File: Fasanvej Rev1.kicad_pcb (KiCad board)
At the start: 2 copper layers, 282 parts, among them J1 Molex 676430910, J10 I meas., J11 I meas., J12 USB4085-GF-A, J2 Molex 676430910, J3 LCD_RGB_40P, J4 Micro_SD_Card, J5 UART console, J6 Serial Wire Debug, J7 I meas., J8 I meas., J9 I meas., Q1 DMN2046U-7, Q2 DMN2046U-7, Q3 DMP2120U-7, SW1 TL3342F260QG, SW10 SW_Push, SW11 SW_Push, SW12 SW_Push, SW13 SW_Push, SW14 SW_Push, SW15 SW_Push, SW16 SW_Push, SW17 SW_Push, SW18 SW_Push, SW19 SW_Push, SW2 SW_Push, SW20 SW_Push, SW21 SW_Push, SW22 SW_Push, SW23 SW_Push, SW24 SW_Push, SW25 SW_Push, SW26 SW_Push, SW27 SW_Push, SW28 SW_Push, SW29 SW_Push, SW3 SW_Push, SW30 SW_Push, SW31 SW_Push, SW32 SW_Push, SW33 SW_Push, SW34 SW_Push, SW35 SW_Push, SW36 SW_Push, SW37 SW_Push, SW38 SW_Push, SW39 SW_Push, SW4 SW_Push, SW40 SW_Push, SW41 SW_Push, SW42 SW_Push, SW43 SW_Push, SW44 SW_Push, SW45 SW_Push, SW46 SW_Push, SW47 SW_Push, SW48 SW_Push, SW49 SW_Push, SW5 SW_Push, SW50 SW_Push, SW51 SW_Push, SW52 SW_Push, SW53 SW_Push, SW54 SW_Push, SW55 SW_Push, SW56 SW_Push, SW57 SW_Push, SW58 SW_Push, SW59 SW_Push, SW6 SW_Push, SW60 SW_Push, SW61 SW_Push, SW62 SW_Push, SW63 SW_Push, SW64 SW_Push, SW65 SW_Push, SW66 SW_SPST, SW67 SW_SPST, SW7 SW_Push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

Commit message: Started placing components
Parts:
- moved BT1 90.0 mm to (275.0, 85.0)
- moved BT2 90.0 mm to (297.5, 85.0)
- moved C1 90.0 mm to (137.5, 62.5)
- moved C10 90.0 mm to (138.4, 75.0)
- moved C11 90.0 mm to (145.0, 47.5)
- moved C12 90.0 mm to (137.5, 52.5)
- moved C13 90.0 mm to (147.5, 65.0)
- moved C14 90.0 mm to (139.0, 47.5)
- moved C15 90.0 mm to (142.5, 52.5)
- moved C16 90.0 mm to (137.5, 77.5)
- moved C17 90.0 mm to (149.1, 47.5)
- moved C18 90.0 mm to (150.0, 52.5)
- moved C19 90.0 mm to (137.5, 87.5)
- moved C2 90.0 mm to (145.0, 50.0)
- moved C20 90.0 mm to (147.5, 97.5)
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
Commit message: Made a lot of progress laying out PCB
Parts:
- removed the D16 at (49.7, 119.6)
- removed the D23 at (68.7, 98.5)
- removed the D24 at (116.7, 65.0)
- removed the D31 at (68.7, 101.4)
- removed the D32 at (102.9, 79.1)
- removed the D39 at (59.8, 117.3)
- removed the D40 at (59.1, 108.5)
- removed the D47 at (88.3, 89.1)
- removed the D48 at (74.3, 104.4)
- removed D55, D56, D63, D64: 1N4148, Diode_SMD:D_SOD-323_HandSoldering
- removed the D8 at (64.2, 108.5)
- removed the SW17 at (57.8, 58.2)
- removed the SW24 at (32.7, 80.3)
- removed the SW25 at (86.4, 58.2)
- removed the SW32 at (32.7, 108.5)
- removed the SW33 at (13.6, 113.0)
- removed the SW40 at (13.6, 84.8)
- removed the SW41 at (13.6, 98.9)
- removed the SW48 at (56.6, 72.3)
- removed the SW49 at (51.8, 114.6)
- removed SW56, SW57, SW64, SW65: SW_Push, Button_Switch_SMD:SW_SPST_TL3342
- removed the SW9 at (94.8, 65.3)
- removed TP2, TP3: TestPoint_Small, TestPoint:TestPoint_Pad_D4.0mm
- added J13: I2C keyboard, Connector_PinHeader_2.54mm:PinHeader_2x02_P2.54mm_Vertical, B.Cu at (72.5, 70.6)
- added R43: 4k7, Resistor_SMD:R_0603_1608Metric_Pad0.98x0.95mm_HandSolder, B.Cu at (76.1, 70.6)
- added R44: 4k7, Resistor_SMD:R_0603_1608Metric_Pad0.98x0.95mm_HandSolder, B.Cu at (76.1, 68.1)
- added R45: 22k, Resistor_SMD:R_0603_1608Metric_Pad0.98x0.95mm_HandSolder, F.Cu at (128.8, 15.7)
- BT1, BT2, C1, C10, C11, C12, C13, C14, C15, C16, C17, C18, C19, C2, C20, C22, C23, C24, C25, C26, C27, C28, C29, C3, C30, C31, C32, C33, C34, C35, C36, C37, C38, C39, C4, C40, C41, C42, C43, C44, C45, C46, C47, C5, C6, C7, C8, C9, FB1, J4, J5, J6, J7, J8, L1, L2, L3, L4, L5, LS1, Q1, Q2, Q3, R1, R2, R3, R4, R5, R6, R7, SW1, U1, U10, U11, U12, U13, U2, U3, U4, U5, U6, U7, U8, U9, Y1, Y2: moved to B.Cu
- C48: renamed from C49; moved to B.Cu
- C49: renamed from C50; moved to B.Cu
- C50: renamed from C51; moved to B.Cu
- C51: renamed from C52; moved to B.Cu
- C52: renamed from C53; moved to B.Cu
- C53: renamed from C54; moved to B.Cu
- D53: renamed from D66; moved to B.Cu
- D54: renamed from D67; moved to B.Cu
- J1: renamed from J2; moved to B.Cu
- J10: renamed from J9; moved to B.Cu
- J11: renamed from J10; moved to B.Cu
- J12: renamed from J11; moved to B.Cu
- J2: renamed from J1; moved to B.Cu
- J3: value LCD_RGB_40P -> LQ035NC111; footprint RISRES Library:TE_4-1734839-0_1x40-1MP_P0.5mm_Horizontal -> RISRES Library:FFC2B22-54-T
- J9: renamed from J12; moved to B.Cu
- R10: renamed from R8; moved to B.Cu
- R11: renamed from R9; moved to B.Cu
- R12: renamed from R10; moved to B.Cu
- R13: renamed from R11; moved to B.Cu
- R14: renamed from R12; moved to B.Cu
- R15: renamed from R13; moved to B.Cu
- R16: renamed from R40; moved to B.Cu
- R17: renamed from R41; moved to B.Cu
- R18: renamed from R14; moved to B.Cu
- R19: renamed from R42; moved to B.Cu
- R20: renamed from R15; moved to B.Cu
- R21: renamed from R16; moved to B.Cu
- R22: renamed from R38; moved to B.Cu
- R23: renamed from R39; moved to B.Cu
- R24: renamed from R17; moved to B.Cu
- R25: renamed from R18; moved to B.Cu
- R26: renamed from R19; moved to B.Cu
- R27: renamed from R20; moved to B.Cu
- R28: renamed from R21; moved to B.Cu
- R29: renamed from R22; moved to B.Cu
- R30: renamed from R23; moved to B.Cu
- R31: renamed from R24; moved to B.Cu
- R32: renamed from R25; moved to B.Cu
- R33: renamed from R26; moved to B.Cu
- R34: renamed from R27; moved to B.Cu
- R35: renamed from R28; moved to B.Cu
- R36: renamed from R29; moved to B.Cu
- R37: renamed from R30; moved to B.Cu
- R38: renamed from R31; moved to B.Cu
- R39: renamed from R32; moved to B.Cu
- R40: renamed from R33; moved to B.Cu
- R41: renamed from R34; moved to B.Cu
- R42: renamed from R35; moved to B.Cu
- R8: renamed from R36; moved to B.Cu
- R9: renamed from R37; moved to B.Cu
- SW10: renamed from SW11; value SW_Push -> W
- SW11: renamed from SW12; value SW_Push -> S
- SW12: renamed from SW13; value SW_Push -> X
- SW13: renamed from SW14; value SW_Push -> tab
- SW14: renamed from SW15; value SW_Push -> 0
- SW15: renamed from SW16; value SW_Push -> enter
- SW16: renamed from SW18; value SW_Push -> 3
- SW17: renamed from SW19; value SW_Push -> E
- SW18: renamed from SW20; value SW_Push -> D
- SW19: renamed from SW21; value SW_Push -> C
- SW2: value SW_Push -> 1
- SW20: renamed from SW22; value SW_Push -> caps lock
- SW21: renamed from SW23; value SW_Push -> O
- SW22: renamed from SW26; value SW_Push -> 4
- SW23: renamed from SW27; value SW_Push -> R
- SW24: renamed from SW28; value SW_Push -> F
- SW25: renamed from SW29; value SW_Push -> V
- SW26: renamed from SW30; value SW_Push -> ctrl
- SW27: renamed from SW31; value SW_Push -> P
- SW28: renamed from SW34; value SW_Push -> 5
- SW29: renamed from SW35; value SW_Push -> T
- SW3: value SW_Push -> Q
- SW30: renamed from SW36; value SW_Push -> G
- SW31: renamed from SW37; value SW_Push -> B
- SW32: renamed from SW38; value SW_Push -> space
- SW33: renamed from SW39; value SW_Push -> L
- SW34: renamed from SW42; value SW_Push -> 6
- SW35: renamed from SW43; value SW_Push -> Y
- SW36: renamed from SW44; value SW_Push -> H
- SW37: renamed from SW45; value SW_Push -> N
- SW38: renamed from SW46; value SW_Push -> space
- SW39: renamed from SW47; value SW_Push -> star
- SW4: value SW_Push -> A
- SW40: renamed from SW50; value SW_Push -> 7
- SW41: renamed from SW51; value SW_Push -> U
- SW42: renamed from SW52; value SW_Push -> J
- SW43: renamed from SW53; value SW_Push -> M
- SW44: renamed from SW54; value SW_Push -> empty
- SW45: renamed from SW55; value SW_Push -> point
- SW46: renamed from SW58; value SW_Push -> 8
- SW47: renamed from SW59; value SW_Push -> I
- SW48: renamed from SW60; value SW_Push -> K
- SW49: renamed from SW61; value SW_Push -> comma
- SW5: value SW_Push -> Z
- SW50: renamed from SW62; value SW_Push -> alt
- SW51: renamed from SW63; value SW_Push -> dash
- SW6: value SW_Push -> shift
- SW7: value SW_Push -> 9
- SW8: value SW_Push -> enter
- SW9: renamed from SW10; value SW_Push -> 2
- moved R16 252.6 mm to (13.8, 9.50), turned to 90 degrees
- moved J9 250.3 mm to (12.0, 6.53)
- moved R19 242.3 mm to (18.8, 8.50)
- moved R17 240.7 mm to (22.2, 3.75), turned to 180 degrees
- moved D52 237.7 mm to (26.6, 2.50)
- moved BT1 234.9 mm to (45.0, 37.5), turned to 180 degrees
- moved D51 228.9 mm to (30.6, 2.50)
- moved D6 218.8 mm to (200.5, 11.5), turned to -90 degrees
- moved H1 215.2 mm to (5.00, 5.00)
- moved R9 203.2 mm to (217.2, 51.8), turned to 180 degrees
- moved SW51 198.4 mm to (207.5, 50.0)
- moved R23 195.7 mm to (53.2, 2.50), turned to 180 degrees
- moved R22 194.3 mm to (49.8, 2.50)
- moved SW21 194.2 mm to (195.0, 25.0)
- moved Q3 194.0 mm to (50.8, 5.00), turned to 180 degrees
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- renumbered D11 to D10, D12 to D11, D13 to D12, D14 to D13, D15 to D14, D17 to D15, D18 to D16, D19 to D17, D20 to D18, D21 to D19, D22 to D20, D25 to D21, D26 to D22, D27 to D23, D28 to D24, D29 to D25, D30 to D26, D33 to D27, D34 to D28, D35 to D29, D36 to D30, D37 to D31, D38 to D32, D41 to D33, D42 to D34, D43 to D35, D44 to D36, D45 to D37, D46 to D38, D49 to D39, D50 to D40, D51 to D41, D52 to D42, D53 to D43, D54 to D44, D57 to D45, D58 to D46, D59 to D47, D60 to D48, D61 to D49, D62 to D50, D65 to D51, D68 to D52, D9 to D8, D10 to D9, SW67 to SW52, SW66 to SW53
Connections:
- C23 pad 1: Net-(C23-Pad1) -> /Keyboard/+3V3_SAMD21
- C24 pad 1: Net-(C23-Pad1) -> /Keyboard/+3V3_SAMD21
- C25 pad 1: Net-(C23-Pad1) -> /Keyboard/+3V3_SAMD21
- C26 pad 1: Net-(C23-Pad1) -> /Keyboard/+3V3_SAMD21
- C27 pad 1: Net-(C23-Pad1) -> /Keyboard/+3V3_SAMD21
- C28 pad 1: Net-(C23-Pad1) -> /Keyboard/+3V3_SAMD21
- C29 pad 1: Net-(C23-Pad1) -> /Keyboard/+3V3_SAMD21
- D1 pad 1: /Keyboard/ROW_1 -> /Keyboard/COLUMN_1
- D10 pad 1: /Keyboard/ROW_3 -> /Keyboard/COLUMN_3
- D11 pad 1: /Keyboard/ROW_4 -> /Keyboard/COLUMN_4
- D12 pad 1: /Keyboard/ROW_5 -> /Keyboard/COLUMN_5
- D13 pad 1: /Keyboard/ROW_6 -> /Keyboard/COLUMN_6
- D14 pad 1: /Keyboard/ROW_7 -> /Keyboard/COLUMN_7
- D15 pad 1: /Keyboard/ROW_1 -> /Keyboard/COLUMN_1
- D16 pad 1: /Keyboard/ROW_2 -> /Keyboard/COLUMN_2
- D17 pad 1: /Keyboard/ROW_3 -> /Keyboard/COLUMN_3
- D18 pad 1: /Keyboard/ROW_4 -> /Keyboard/COLUMN_4
- D19 pad 1: /Keyboard/ROW_5 -> /Keyboard/COLUMN_5
- D2 pad 1: /Keyboard/ROW_2 -> /Keyboard/COLUMN_2
- D20 pad 1: /Keyboard/ROW_6 -> /Keyboard/COLUMN_6
- D21 pad 1: /Keyboard/ROW_1 -> /Keyboard/COLUMN_1
- D22 pad 1: /Keyboard/ROW_2 -> /Keyboard/COLUMN_2
- D23 pad 1: /Keyboard/ROW_3 -> /Keyboard/COLUMN_3
- D24 pad 1: /Keyboard/ROW_4 -> /Keyboard/COLUMN_4
- D25 pad 1: /Keyboard/ROW_5 -> /Keyboard/COLUMN_5
- D26 pad 1: /Keyboard/ROW_6 -> /Keyboard/COLUMN_6
- D27 pad 1: /Keyboard/ROW_1 -> /Keyboard/COLUMN_1
- D28 pad 1: /Keyboard/ROW_2 -> /Keyboard/COLUMN_2
- D29 pad 1: /Keyboard/ROW_3 -> /Keyboard/COLUMN_3
- D3 pad 1: /Keyboard/ROW_3 -> /Keyboard/COLUMN_3
- D30 pad 1: /Keyboard/ROW_4 -> /Keyboard/COLUMN_4
- D31 pad 1: /Keyboard/ROW_5 -> /Keyboard/COLUMN_5
- D32 pad 1: /Keyboard/ROW_6 -> /Keyboard/COLUMN_6
- D33 pad 1: /Keyboard/ROW_1 -> /Keyboard/COLUMN_1
- D34 pad 1: /Keyboard/ROW_2 -> /Keyboard/COLUMN_2
- D35 pad 1: /Keyboard/ROW_3 -> /Keyboard/COLUMN_3
- D36 pad 1: /Keyboard/ROW_4 -> /Keyboard/COLUMN_4
- D37 pad 1: /Keyboard/ROW_5 -> /Keyboard/COLUMN_5
- D38 pad 1: /Keyboard/ROW_6 -> /Keyboard/COLUMN_6
- D39 pad 1: /Keyboard/ROW_1 -> /Keyboard/COLUMN_1
- D4 pad 1: /Keyboard/ROW_4 -> /Keyboard/COLUMN_4
- D40 pad 1: /Keyboard/ROW_2 -> /Keyboard/COLUMN_2
- D41 pad 1: /Keyboard/ROW_3 -> /Keyboard/COLUMN_3
- D42 pad 1: /Keyboard/ROW_4 -> /Keyboard/COLUMN_4
- D43 pad 1: /Keyboard/ROW_5 -> /Keyboard/COLUMN_5
- D44 pad 1: /Keyboard/ROW_6 -> /Keyboard/COLUMN_6
- D45 pad 1: /Keyboard/ROW_1 -> /Keyboard/COLUMN_1
- D46 pad 1: /Keyboard/ROW_2 -> /Keyboard/COLUMN_2
- D47 pad 1: /Keyboard/ROW_3 -> /Keyboard/COLUMN_3
- D48 pad 1: /Keyboard/ROW_4 -> /Keyboard/COLUMN_4
- D49 pad 1: /Keyboard/ROW_5 -> /Keyboard/COLUMN_5
- D5 pad 1: /Keyboard/ROW_5 -> /Keyboard/COLUMN_5
- D50 pad 1: /Keyboard/ROW_6 -> /Keyboard/COLUMN_6
- D6 pad 1: /Keyboard/ROW_6 -> /Keyboard/COLUMN_6
- D7 pad 1: /Keyboard/ROW_7 -> /Keyboard/COLUMN_7
- D8 pad 1: /Keyboard/ROW_1 -> /Keyboard/COLUMN_1
- D9 pad 1: /Keyboard/ROW_2 -> /Keyboard/COLUMN_2
- FB1 pad 2: Net-(C23-Pad1) -> /Keyboard/+3V3_SAMD21
- J1 pad 2: Net-(J2-Pad2) -> Net-(J1-Pad2)
- J1 pad 3: Net-(J2-Pad3) -> Net-(J1-Pad3)
- J3 pad 10: /LCD_D21 -> Net-(J3-Pad10)
- J3 pad 11: /LCD_D22 -> Net-(J3-Pad10)
- J3 pad 12: /LCD_D23 -> GND
- J3 pad 14: GND -> /LCD_D2
- J3 pad 15: /LCD_D10 -> /LCD_D3
- J3 pad 16: /LCD_D11 -> /LCD_D4
- J3 pad 17: /LCD_D12 -> /LCD_D5
- J3 pad 18: /LCD_D13 -> /LCD_D6
- J3 pad 19: /LCD_D14 -> /LCD_D7
- J3 pad 2: LED_BACKLIGHT_A -> LED_BACKLIGHT_K
- J3 pad 20: /LCD_D15 -> GND
- J3 pad 22: GND -> /LCD_D10
- J3 pad 23: /LCD_D2 -> /LCD_D11
- J3 pad 24: /LCD_D3 -> /LCD_D12
- J3 pad 25: /LCD_D4 -> /LCD_D13
- J3 pad 26: /LCD_D5 -> /LCD_D14
- J3 pad 27: /LCD_D6 -> /LCD_D15
- J3 pad 28: /LCD_D7 -> GND
- J3 pad 3: GND -> LED_BACKLIGHT_A
- J3 pad 30: /LCD_CLK -> /LCD_D23
- J3 pad 31: +3V3 -> /LCD_D22
- J3 pad 32: /LCD_HSYNC -> /LCD_D21
- J3 pad 33: /LCD_VSYNC -> /LCD_D20
- J3 pad 34: /LCD_DE -> /LCD_D19
- J3 pad 35: (no net) -> /LCD_D18
- J3 pad 36: GND -> /LCD_HSYNC
- J3 pad 37: /TPX1 -> /LCD_VSYNC
- J3 pad 38: /TPY1 -> /LCD_CLK
- J3 pad 39: /TPX2 -> unconnected-(J3-Pad39)
- J3 pad 4: +3V3 -> LED_BACKLIGHT_A
- J3 pad 40: /TPY2 -> unconnected-(J3-Pad40)
- J3 pad 5: GND -> unconnected-(J3-Pad5)
- J3 pad 6: GND -> unconnected-(J3-Pad6)
- J3 pad 7: /LCD_D18 -> unconnected-(J3-Pad7)
- J3 pad 8: /LCD_D19 -> Net-(J3-Pad10)
- J3 pad 9: /LCD_D20 -> Net-(J3-Pad10)
- J6 pad 1: +3V3 -> /Keyboard/+3V3_SAMD21
- R6 pad 1: +3V3 -> /Keyboard/+3V3_SAMD21
- R7 pad 1: +3V3 -> /Keyboard/+3V3_SAMD21
- R9 pad 1: +3V3 -> Net-(R9-Pad1)
- R9 pad 2: Net-(R37-Pad2) -> /Keyboard/+3V3_SAMD21
- SW10 pad 2: /Keyboard/COLUMN_2 -> /Keyboard/ROW_2
- SW11 pad 2: /Keyboard/COLUMN_2 -> /Keyboard/ROW_2
- SW12 pad 2: /Keyboard/COLUMN_2 -> /Keyboard/ROW_2
- SW13 pad 2: /Keyboard/COLUMN_2 -> /Keyboard/ROW_2
- SW14 pad 2: /Keyboard/COLUMN_2 -> /Keyboard/ROW_2
- SW15 pad 2: /Keyboard/COLUMN_2 -> /Keyboard/ROW_2
- SW16 pad 2: /Keyboard/COLUMN_3 -> /Keyboard/ROW_3
- SW17 pad 2: /Keyboard/COLUMN_3 -> /Keyboard/ROW_3
- SW18 pad 2: /Keyboard/COLUMN_3 -> /Keyboard/ROW_3
- SW19 pad 2: /Keyboard/COLUMN_3 -> /Keyboard/ROW_3
- SW2 pad 2: /Keyboard/COLUMN_1 -> /Keyboard/ROW_1
- SW20 pad 2: /Keyboard/COLUMN_3 -> /Keyboard/ROW_3
- SW21 pad 2: /Keyboard/COLUMN_3 -> /Keyboard/ROW_3
- SW22 pad 2: /Keyboard/COLUMN_4 -> /Keyboard/ROW_4
- SW23 pad 2: /Keyboard/COLUMN_4 -> /Keyboard/ROW_4
- SW24 pad 2: /Keyboard/COLUMN_4 -> /Keyboard/ROW_4
- SW25 pad 2: /Keyboard/COLUMN_4 -> /Keyboard/ROW_4
- SW26 pad 2: /Keyboard/COLUMN_4 -> /Keyboard/ROW_4
- SW27 pad 2: /Keyboard/COLUMN_4 -> /Keyboard/ROW_4
- SW28 pad 2: /Keyboard/COLUMN_5 -> /Keyboard/ROW_5
- SW29 pad 2: /Keyboard/COLUMN_5 -> /Keyboard/ROW_5
- SW3 pad 2: /Keyboard/COLUMN_1 -> /Keyboard/ROW_1
- SW30 pad 2: /Keyboard/COLUMN_5 -> /Keyboard/ROW_5
- SW31 pad 2: /Keyboard/COLUMN_5 -> /Keyboard/ROW_5
- SW32 pad 2: /Keyboard/COLUMN_5 -> /Keyboard/ROW_5
- SW33 pad 2: /Keyboard/COLUMN_5 -> /Keyboard/ROW_5
- SW34 pad 2: /Keyboard/COLUMN_6 -> /Keyboard/ROW_6
- SW35 pad 2: /Keyboard/COLUMN_6 -> /Keyboard/ROW_6
- SW36 pad 2: /Keyboard/COLUMN_6 -> /Keyboard/ROW_6
- SW37 pad 2: /Keyboard/COLUMN_6 -> /Keyboard/ROW_6
- SW38 pad 2: /Keyboard/COLUMN_6 -> /Keyboard/ROW_6
- SW39 pad 2: /Keyboard/COLUMN_6 -> /Keyboard/ROW_6
- SW4 pad 2: /Keyboard/COLUMN_1 -> /Keyboard/ROW_1
- SW40 pad 2: /Keyboard/COLUMN_7 -> /Keyboard/ROW_7
- SW41 pad 2: /Keyboard/COLUMN_7 -> /Keyboard/ROW_7
- SW42 pad 2: /Keyboard/COLUMN_7 -> /Keyboard/ROW_7
- SW43 pad 2: /Keyboard/COLUMN_7 -> /Keyboard/ROW_7
- SW44 pad 2: /Keyboard/COLUMN_7 -> /Keyboard/ROW_7
- SW45 pad 2: /Keyboard/COLUMN_7 -> /Keyboard/ROW_7
- SW46 pad 2: /Keyboard/COLUMN_8 -> /Keyboard/ROW_8
- SW47 pad 2: /Keyboard/COLUMN_8 -> /Keyboard/ROW_8
- SW48 pad 2: /Keyboard/COLUMN_8 -> /Keyboard/ROW_8
- SW49 pad 2: /Keyboard/COLUMN_8 -> /Keyboard/ROW_8
- SW5 pad 2: /Keyboard/COLUMN_1 -> /Keyboard/ROW_1
- SW50 pad 2: /Keyboard/COLUMN_8 -> /Keyboard/ROW_8
- SW51 pad 2: /Keyboard/COLUMN_8 -> /Keyboard/ROW_8
- SW52 pad 2: Net-(R37-Pad2) -> Net-(R9-Pad1)
- SW6 pad 2: /Keyboard/COLUMN_1 -> /Keyboard/ROW_1
- SW7 pad 2: /Keyboard/COLUMN_1 -> /Keyboard/ROW_1
- SW8 pad 2: /Keyboard/COLUMN_1 -> /Keyboard/ROW_1
- SW9 pad 2: /Keyboard/COLUMN_2 -> /Keyboard/ROW_2
- TP1 pad 1: /I2C_SCL -> /LCD_D11
- U2 pad 1: /USB_DM_EXTERNAL -> /USB_DP_EXTERNAL
- U2 pad 3: /USB_DP_EXTERNAL -> /USB_DM_EXTERNAL
- U2 pad 4: Net-(J2-Pad3) -> Net-(J1-Pad2)
- U2 pad 6: Net-(J2-Pad2) -> Net-(J1-Pad3)
- U4 pad 21: Net-(C23-Pad1) -> /Keyboard/+3V3_SAMD21
- U4 pad 34: Net-(C23-Pad1) -> /Keyboard/+3V3_SAMD21
- U4 pad 35: unconnected-(U4-Pad35) -> /KEYBOARD_S1_P0
- U4 pad 36: unconnected-(U4-Pad36) -> /KEYBOARD_S1_P1
- U4 pad 48: Net-(C23-Pad1) -> /Keyboard/+3V3_SAMD21
- U4 pad 55: Net-(C23-Pad1) -> /Keyboard/+3V3_SAMD21
- U4 pad 56: Net-(C23-Pad1) -> /Keyboard/+3V3_SAMD21
- U4 pad 8: Net-(C23-Pad1) -> /Keyboard/+3V3_SAMD21
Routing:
- net Net-(BT1-Pad2): track 0.00 -> 175.3 mm
- net /Keyboard/ROW_2: track 0.00 -> 147.8 mm, vias 0 -> 1
- net /Keyboard/ROW_1: track 0.00 -> 137.9 mm, vias 0 -> 1
- net /Keyboard/ROW_3: track 0.00 -> 115.4 mm, vias 0 -> 8
- net /Keyboard/ROW_4: track 0.00 -> 99.2 mm, vias 0 -> 8
- net /Keyboard/ROW_5: track 0.00 -> 97.2 mm, vias 0 -> 8
- net /Keyboard/+3V3_SAMD21: track 0.00 -> 70.7 mm
- net /USB_VBUS_EXTERNAL: track 0.00 -> 67.2 mm, vias 0 -> 1
- net GND: track 0.00 -> 51.1 mm, vias 0 -> 12
- net /Keyboard/COLUMN_5: track 0.00 -> 50.0 mm
- net /Keyboard/COLUMN_4: track 0.00 -> 50.0 mm
- net /Keyboard/COLUMN_3: track 0.00 -> 50.0 mm
- net /Keyboard/COLUMN_2: track 0.00 -> 50.0 mm
- net /Keyboard/COLUMN_1: track 0.00 -> 50.0 mm
- net /Keyboard/SWD_CLK: track 0.00 -> 45.6 mm, vias 0 -> 1
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- added copper zone on B.Cu, net +BATT
- added copper zone on B.Cu, net Net-(D54-Pad2)
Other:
- board outline added: 220 x 72.5 mm

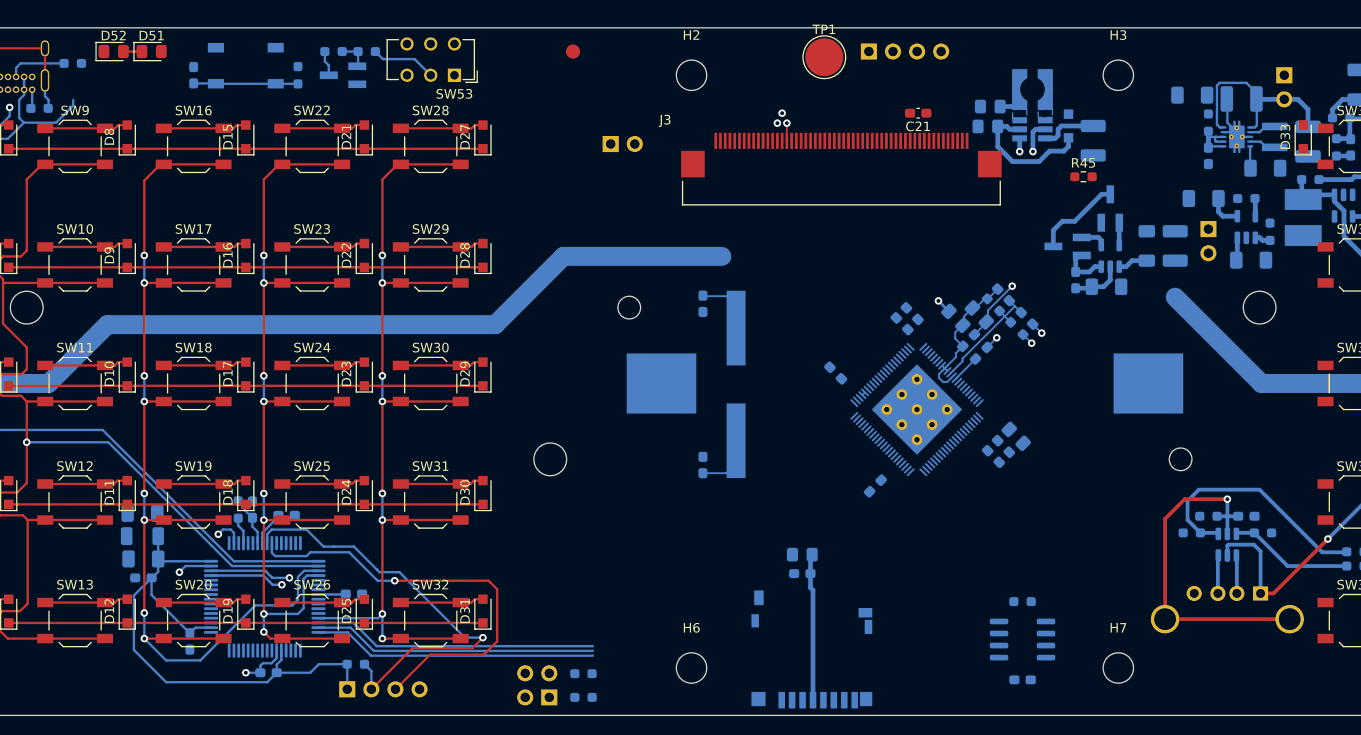
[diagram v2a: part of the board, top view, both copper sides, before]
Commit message: Made progress with board layout as well as mechanical (case) design
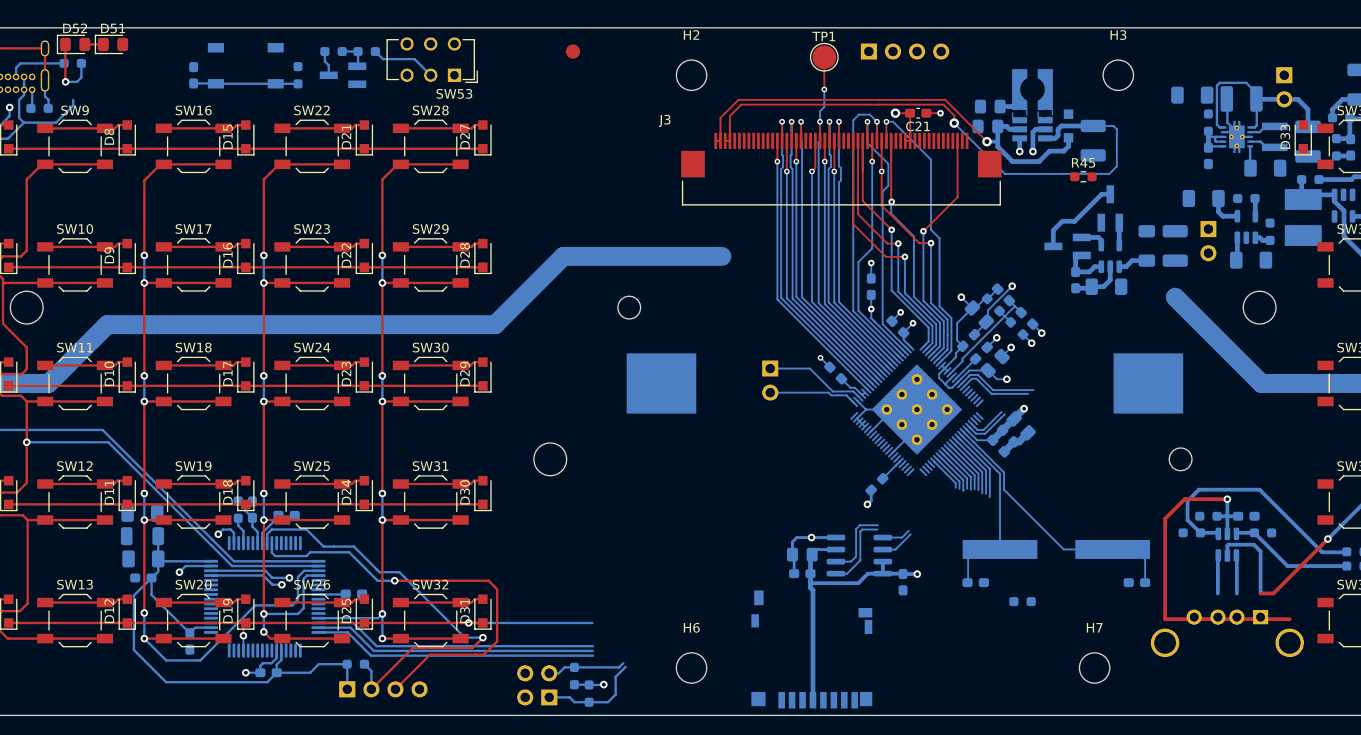
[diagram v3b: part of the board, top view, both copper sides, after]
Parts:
- TP1: footprint TestPoint:TestPoint_Pad_D4.0mm -> TestPoint:TestPoint_Pad_D2.5mm
- moved C6 47.4 mm to (134.5, 58.5), turned to 180 degrees
- moved C5 41.1 mm to (117.5, 58.5), turned to 0 degrees
- moved Y1 38.0 mm to (126.0, 55.0), turned to 180 degrees
- moved LS1 29.0 mm to (95.8, 35.9), turned to 180 degrees
- moved U3 19.3 mm to (105.2, 55.6), turned to 0 degrees
- moved C13 16.3 mm to (109.8, 58.5), turned to -90 degrees
- moved C12 6.31 mm to (119.5, 35.4), turned to -135 degrees
- moved C17 5.08 mm to (106.5, 27.3), turned to -90 degrees
- moved D51 4.14 mm to (26.5, 1.75)
- moved D52 4.14 mm to (22.5, 1.75)
- moved H7 2.50 mm to (130.0, 67.5)
- moved J1 2.50 mm to (147.5, 62.1)
- moved C7 2.07 mm to (109.2, 31.6)
- moved C14 1.22 mm to (122.3, 42.0)
- moved C16 1.22 mm to (119.8, 44.1)
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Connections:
- net Net-(C3-Pad2) renamed /RESET
- net Net-(C5-Pad1) renamed /HOSCO
- net Net-(C6-Pad1) renamed /HOSCI
- U1 pad 63: /TPY2 -> unconnected-(U1-Pad63)
- U1 pad 64: /TPY1 -> unconnected-(U1-Pad64)
- U1 pad 65: /TPX2 -> unconnected-(U1-Pad65)
- U1 pad 66: /TPX1 -> unconnected-(U1-Pad66)
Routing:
- net LED_BACKLIGHT_A: track 5.97 -> 60.8 mm, vias 0 -> 1
- net +3V3: track 15.9 -> 58.1 mm, vias 0 -> 5
- net GND: track 51.1 -> 91.7 mm, vias 12 -> 19
- net /LCD_D11: track 0.00 -> 38.3 mm, vias 0 -> 2
- net LED_BACKLIGHT_K: track 14.2 -> 49.1 mm, vias 0 -> 1
- net /LCD_D3: track 0.00 -> 34.0 mm
- net /LCD_D5: track 0.07 -> 33.3 mm, vias 0 -> 1
- net /LCD_D7: track 0.00 -> 32.4 mm, vias 0 -> 1
- net /LCD_D18: track 0.00 -> 32.1 mm, vias 0 -> 1
- net /LCD_VSYNC: track 0.00 -> 31.2 mm, vias 0 -> 1
- net /LCD_D13: track 0.00 -> 30.7 mm, vias 0 -> 1
- net /LCD_D2: track 0.00 -> 30.2 mm
- net /LCD_D15: track 0.00 -> 29.9 mm, vias 0 -> 1
- net /LCD_D6: track 0.00 -> 28.7 mm, vias 0 -> 1
- net /LCD_D20: track 0.00 -> 28.3 mm, vias 0 -> 1
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
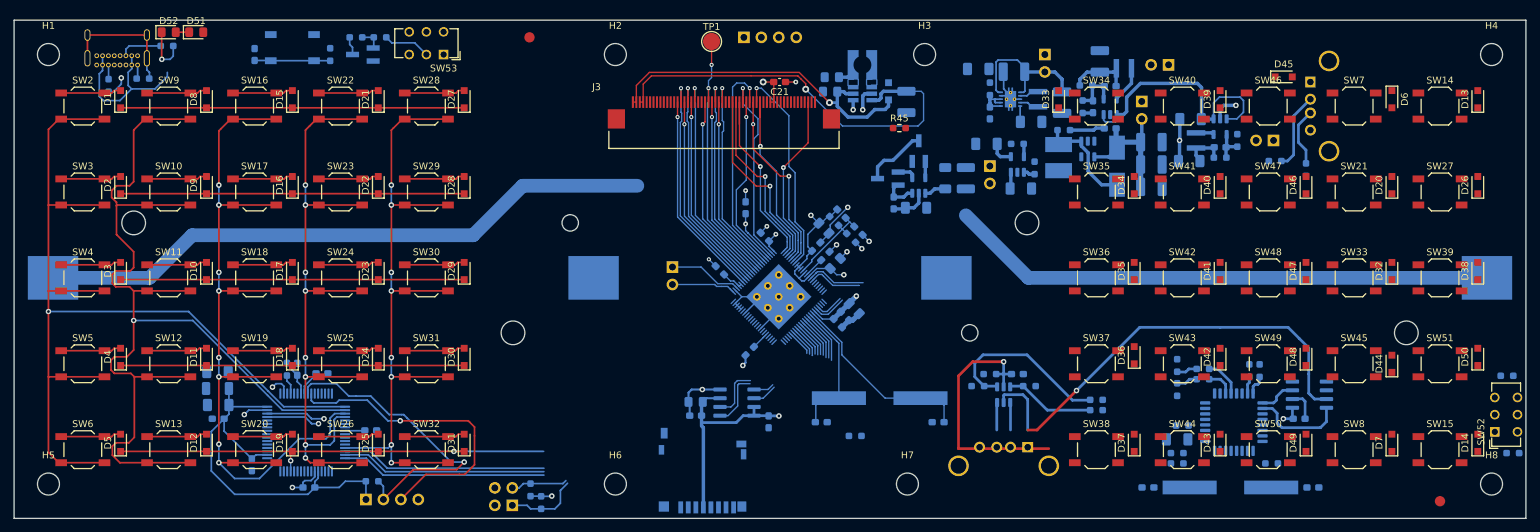
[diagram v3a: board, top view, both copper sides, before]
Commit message: Made progress with PCB layout. Preliminary case design added.
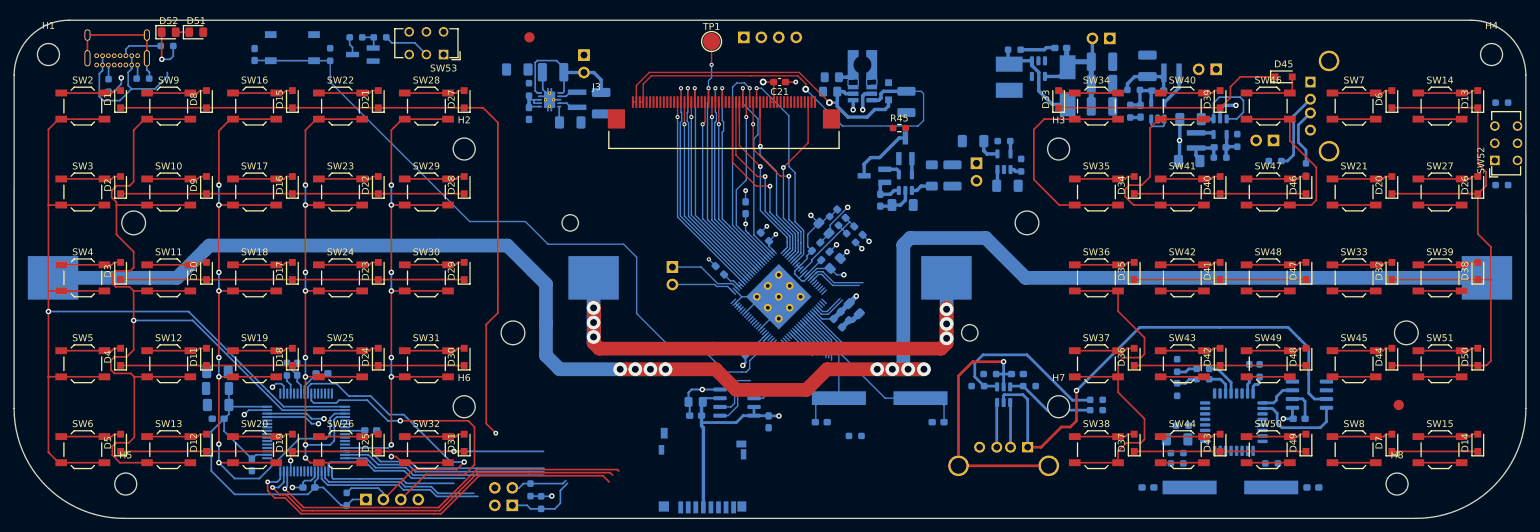
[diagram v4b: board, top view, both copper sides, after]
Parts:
- moved C37 67.1 mm to (73.2, 7.18)
- moved C31 67.1 mm to (80.9, 14.9)
- moved C32 67.1 mm to (74.9, 13.6)
- moved C34 67.1 mm to (78.4, 7.58)
- moved C36 67.1 mm to (85.4, 12.1)
- moved J8 67.1 mm to (82.9, 5.08)
- moved L1 67.1 mm to (81.9, 12.7)
- moved R10 67.1 mm to (74.9, 10.1)
- moved U6 67.1 mm to (77.9, 11.6)
- moved R9 39.8 mm to (216.5, 12.0)
- moved SW52 39.5 mm to (215.5, 20.4)
- moved R8 39.0 mm to (216.5, 24.0)
- moved H2 25.9 mm to (65.5, 18.8)
- moved H6 24.7 mm to (65.5, 56.2)
- moved H7 24.7 mm to (152.0, 56.2)
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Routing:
- net /Keyboard/COLUMN_6: track 0.00 -> 147.5 mm, vias 0 -> 1
- net /Keyboard/COLUMN_1: track 50.0 -> 155.6 mm, vias 0 -> 1
- net Net-(BT1-Pad2): track 175.3 -> 269.0 mm, vias 0 -> 8
- net /Keyboard/ROW_6: track 30.0 -> 123.2 mm
- net /RESET: track 11.0 -> 103.5 mm
- net Net-(BT1-Pad1): track 0.00 -> 80.8 mm, vias 0 -> 6
- net /Keyboard/COLUMN_7: track 0.00 -> 69.4 mm, vias 0 -> 1
- net /Keyboard/COLUMN_8: track 0.00 -> 58.2 mm, vias 0 -> 1
- net /Keyboard/ROW_7: track 30.0 -> 88.0 mm
- net /Keyboard/ROW_8: track 30.0 -> 85.3 mm
- net /Keyboard/COLUMN_4: track 50.0 -> 99.9 mm
- net /Keyboard/COLUMN_3: track 50.0 -> 98.5 mm
- net /Keyboard/COLUMN_2: track 50.0 -> 97.0 mm
- net /Keyboard/COLUMN_5: track 66.1 -> 91.1 mm
- net /Power/BATT_SWITCHED: track 40.0 -> 19.7 mm
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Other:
- outline, holes or cut-outs redrawn
